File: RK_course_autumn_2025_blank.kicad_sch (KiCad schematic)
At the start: 13 parts, among them J1 JST-ZH 6pin, J2 JST-ZH 6pin, J3 Conn_01x02, J4 JST-ZH 6pin, J5 JST-ZH 6pin

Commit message: update
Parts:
- added R1: R, Resistor_SMD:R_0603_1608Metric_Pad0.98x0.95mm_HandSolder, symbol Device:R
- A2: footprint KURSUS:ESP32-S3-DevKitC-1 -> RK_COURSE:ESP32-S3-DevKitC-1
- U4, U6: footprint TANK:TB6612FNG_DUAL_MOTOR_DRIVER_RED -> KURSUS:TB6612FNG_DUAL_MOTOR_DRIVER_RED
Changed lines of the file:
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@@
 			)
 		)
-		(property "Footprint" "KURSUS:ESP32-S3-DevKitC-1"
+		(property "Footprint" "RK_COURSE:ESP32-S3-DevKitC-1"
 			(at 172.72 51.308 0)
 			(effects
@@
 				(path "/a85e8d7d-6e69-4ae0-af3b-65bd111e6aa4"
 					(reference "#PWR02")
-					(unit 1)
-				)
-			)
-		)
-	)
-	(symbol
-		(lib_id "Kursus:TB6612FNG_MOTOR_DRIVER_RED")
-		(at 152.4 78.74 0)
-		(unit 1)
-		(exclude_from_sim no)
-		(in_bom yes)
-		(on_board yes)
-		(dnp no)
-		(property "Reference" "U6"
-			(at 154.94 76.454 0)
-			(effects
-				(font
-					(size 1.27 1.27)
-				)
-			)
-		)
-		(property "Value" "~"
-			(at 152.4 76.2 0)
-			(effects
-				(font
-					(size 1.27 1.27)
-				)
-			)
-		)
-		(property "Footprint" "TANK:TB6612FNG_DUAL_MOTOR_DRIVER_RED"
-			(at 152.4 75.565 0)
-			(effects
-				(font
-					(size 1.27 1.27)
-				)
-				(hide yes)
-			)
-		)
-		(property "Datasheet" ""
-			(at 152.4 75.565 0)
-			(effects
-				(font
-					(size 1.27 1.27)
-				)
-				(hide yes)
-			)
-		)
-		(property "Description" ""
-			(at 152.4 75.565 0)
-			(effects
-				(font
-					(size 1.27 1.27)
-				)
-				(hide yes)
-			)
-		)
-		(pin "15"
-		)
-		(pin "14"
-		)
-		(pin "16"
-		)
-		(pin "1"
-		)
-		(pin "2"
-		)
-		(pin "10"
-		)
-		(pin "5"
-		)
-		(pin "6"
-		)
-		(pin "4"
-		)
-		(pin "9"
-		)
-		(pin "11"
-		)
-		(pin "8"
-		)
-		(pin "12"
-		)
-		(pin "7"
-		)
-		(pin "3"
-		)
-		(pin "13"
-		)
-		(instances
-			(project "RK_course_autumn_2025_blank"
-				(path "/a85e8d7d-6e69-4ae0-af3b-65bd111e6aa4"
-					(reference "U6")
 					(unit 1)
 				)
@@
 	)
 	(symbol
+		(lib_id "Device:R")
+		(at 71.12 27.94 0)
+		(unit 1)
+		(exclude_from_sim no)
+		(in_bom yes)
+		(on_board yes)
+		(dnp no)
+		(fields_autoplaced yes)
+		(property "Reference" "R1"
+			(at 73.66 26.6699 0)
+			(effects
+				(font
+					(size 1.27 1.27)
+				)
+				(justify left)
+			)
+		)
+		(property "Value" "R"
+			(at 73.66 29.2099 0)
+			(effects
+				(font
+					(size 1.27 1.27)
+				)
+				(justify left)
+			)
+		)
+		(property "Footprint" "Resistor_SMD:R_0603_1608Metric_Pad0.98x0.95mm_HandSolder"
+			(at 69.342 27.94 90)
+			(effects
+				(font
+					(size 1.27 1.27)
+				)
+				(hide yes)
+			)
+		)
+		(property "Datasheet" "~"
+			(at 71.12 27.94 0)
+			(effects
+				(font
+					(size 1.27 1.27)
+				)
+				(hide yes)
+			)
+		)
+		(property "Description" "Resistor"
+			(at 71.12 27.94 0)
+			(effects
+				(font
+					(size 1.27 1.27)
+				)
+				(hide yes)
+			)
+		)
+		(pin "1"
+		)
+		(pin "2"
+		)
+		(instances
+			(project ""
+				(path "/a85e8d7d-6e69-4ae0-af3b-65bd111e6aa4"
+					(reference "R1")
+					(unit 1)
+				)
+			)
+		)
+	)
+	(symbol
 		(lib_id "Kursus:PINGEREGU")
 		(at 43.18 26.67 0)
@@
 			)
 		)
-		(property "Footprint" "TANK:TB6612FNG_DUAL_MOTOR_DRIVER_RED"
+		(property "Footprint" "KURSUS:TB6612FNG_DUAL_MOTOR_DRIVER_RED"
 			(at 110.49 75.565 0)
 			(effects
@@
 					(unit 1)
 				)
+			)
+		)
+	)
+	(symbol
+		(lib_id "Kursus:TB6612FNG_MOTOR_DRIVER_RED")
+		(at 152.4 78.74 0)
+		(unit 1)
+		(exclude_from_sim no)
+		(in_bom yes)
+		(on_board yes)
+		(dnp no)
+		(property "Reference" "U6"
+			(at 154.94 76.454 0)
+			(effects
+				(font
+					(size 1.27 1.27)
+				)
+			)
+		)
+		(property "Value" "~"
+			(at 152.4 76.2 0)
+			(effects
+				(font
+					(size 1.27 1.27)
+				)
+			)
+		)
+		(property "Footprint" "KURSUS:TB6612FNG_DUAL_MOTOR_DRIVER_RED"
+			(at 152.4 75.565 0)
+			(effects
+				(font
+					(size 1.27 1.27)
+				)
+				(hide yes)
+			)
+		)
+		(property "Datasheet" ""
+			(at 152.4 75.565 0)
+			(effects
+				(font
+					(size 1.27 1.27)
+				)
+				(hide yes)
+			)
+		)
+		(property "Description" ""
+			(at 152.4 75.565 0)
+			(effects
+				(font
+					(size 1.27 1.27)
+				)
+				(hide yes)
+			)
+		)
+		(pin "15"
+		)
+		(pin "14"
+		)
+		(pin "16"
+		)
+		(pin "1"
+		)
+		(pin "2"
+		)
+		(pin "10"
+		)
+		(pin "5"
+		)
+		(pin "6"
+		)
+		(pin "4"
+		)
+		(pin "9"
+		)
+		(pin "11"
+		)
+		(pin "8"
+		)
+		(pin "12"
+		)
+		(pin "7"
+		)
+		(pin "3"
+		)
+		(pin "13"
+		)
+		(instances
+			(project "RK_course_autumn_2025_blank"
+				(path "/a85e8d7d-6e69-4ae0-af3b-65bd111e6aa4"
+					(reference "U6")
+					(unit 1)
+				)

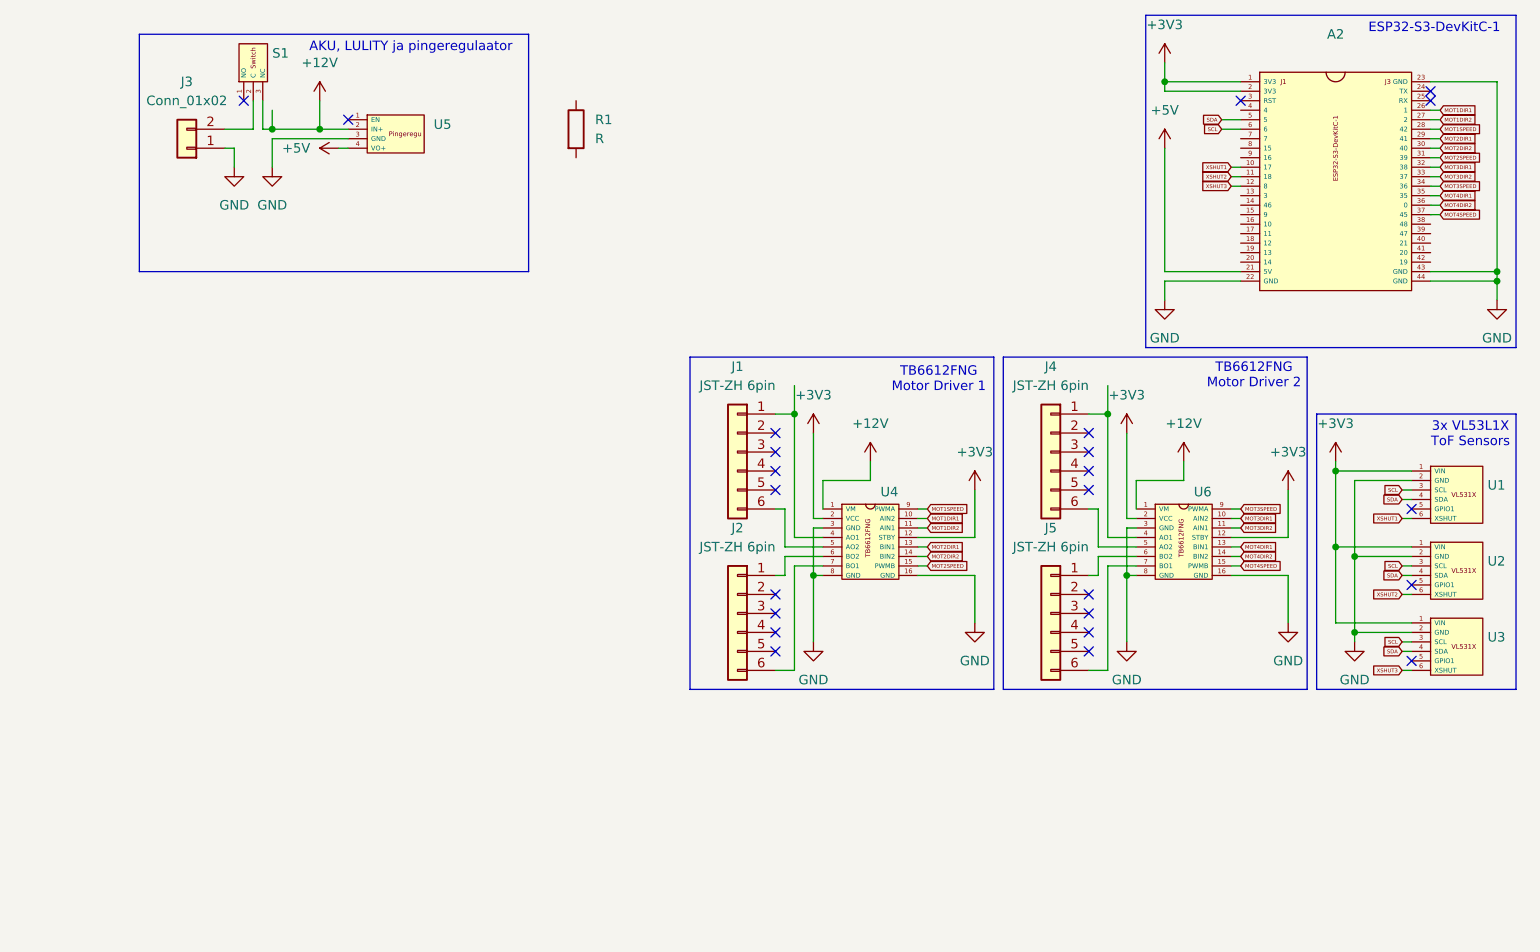
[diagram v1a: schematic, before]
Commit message: Added IMU footprint, model, schematic. Updated the schematic and PCB a bit
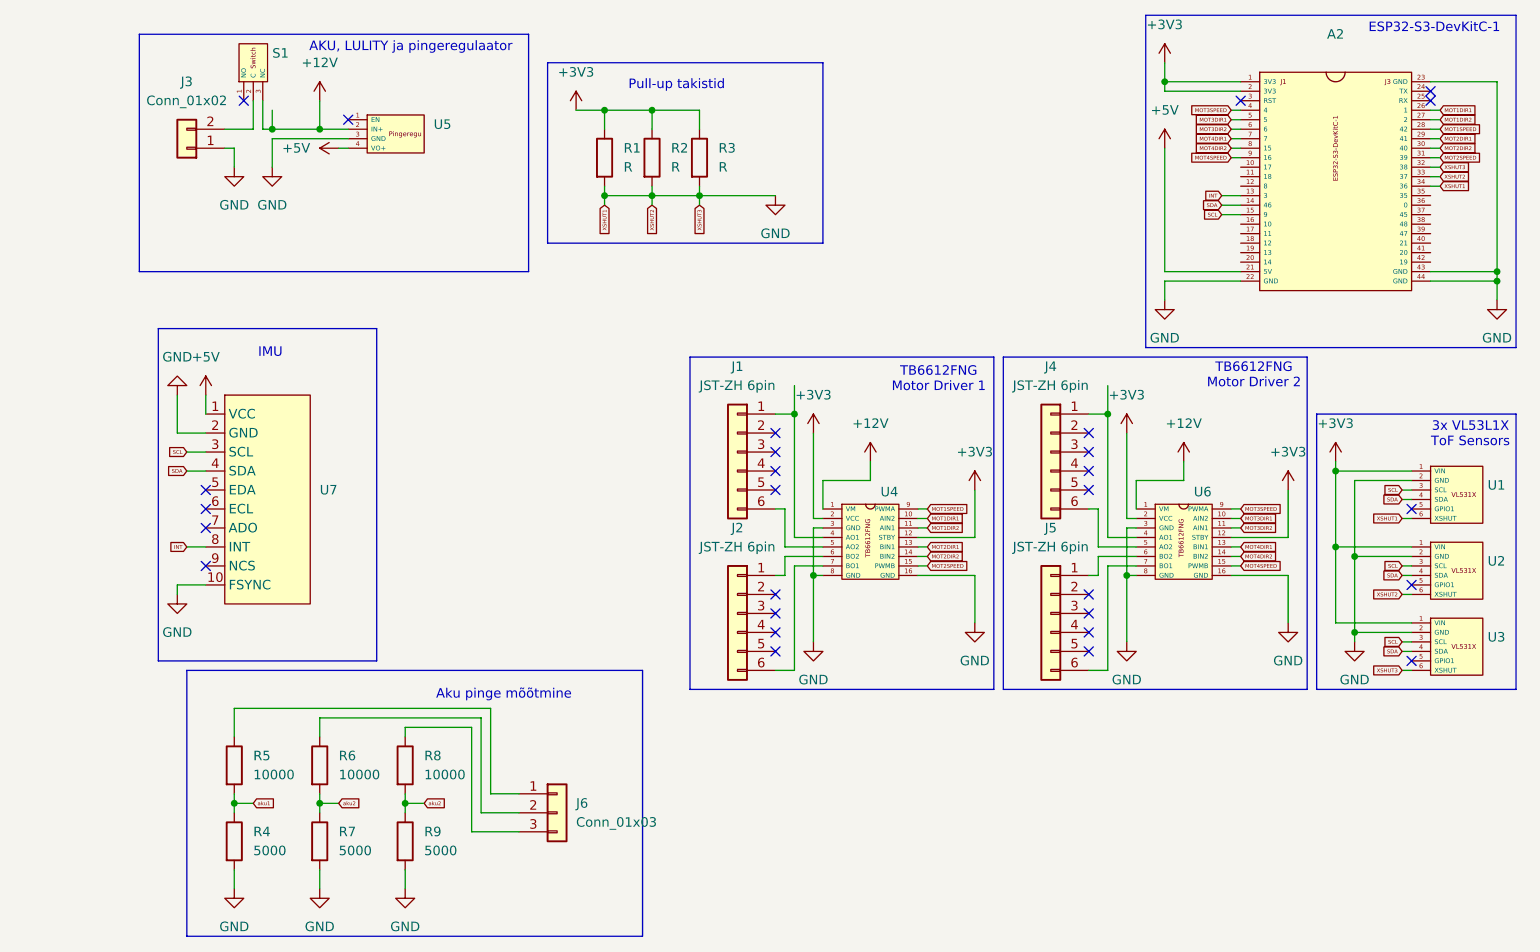
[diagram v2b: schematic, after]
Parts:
- added J6: Conn_01x03, symbol Connector_Generic:Conn_01x03
- added R2, R3: R, Resistor_SMD:R_0603_1608Metric_Pad0.98x0.95mm_HandSolder, symbol Device:R
- added R4, R7, R9: 5000, symbol Device:R
- added R5, R6, R8: 10000, symbol Device:R
- added U7: ~, KURSUS:IMU, symbol Kursus:IMU
- J1, J2, J4, J5: footprint Connector_JST:JST_ZH_B6B-ZR_1x06_P1.50mm_Vertical -> KURSUS:JST_ZH_B6B-ZR_1x06_P1.50mm_Vertical
- J3: footprint Connector_AMASS:AMASS_XT30PW-M_1x02_P2.50mm_Horizontal -> KURSUS:AMASS_XT30PW-M_1x02_P2.50mm_Horizontal
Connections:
- net +3V3: now also R1.1, R2.1, R3.1
- net +5V: now also U7.1 (VCC)
- net GND: now also A2.32 (38), A2.33 (37), A2.34 (36), R1.2, U1.6 (XSHUT), U2.6 (XSHUT), U3.6 (XSHUT), R2.2, R3.2, R4.2, R7.2, R9.2, U7.10 (FSYNC), U7.2 (GND)
- net MOT3DIR1: now also A2.5; no longer A2.32 (38)
- net MOT3DIR2: now also A2.6; no longer A2.33 (37)
- net MOT3SPEED: now also A2.4; no longer A2.34 (36)
- net MOT4DIR1: now also A2.7; no longer A2.35
- net MOT4DIR2: now also A2.8 (15); no longer A2.36 (0)
- net MOT4SPEED: now also A2.9 (16); no longer A2.37 (45)
- net SCL: now also A2.15 (9), U7.3 (SCL); no longer A2.6
- net SDA: now also A2.14 (46), U7.4 (SDA); no longer A2.5
- net INT: now reaches A2.13 (3)
- net INT: now also U7.8 (INT)
- net XSHUT1: no longer names the net of A2.10 (17)
- net XSHUT1: no longer U1.6 (XSHUT)
- net XSHUT2: no longer names the net of A2.11 (18)
- net XSHUT2: no longer U2.6 (XSHUT)
- net XSHUT3: no longer names the net of A2.12 (8)
- net XSHUT3: no longer U3.6 (XSHUT)
- new net: J6.1 (Pin_1), R5.1
- new net: J6.3 (Pin_3), R8.1
- new net: J6.2 (Pin_2), R6.1
- new net aku1: R4.1, R5.2
- new net aku2: R6.2, R7.1, R8.2, R9.1
- no-connect marks 24 -> 28
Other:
- note added: "Aku pinge mõõtmine"
- note added: "IMU"
- note added: "Pull-up takistid"
- moved on the sheet: R1

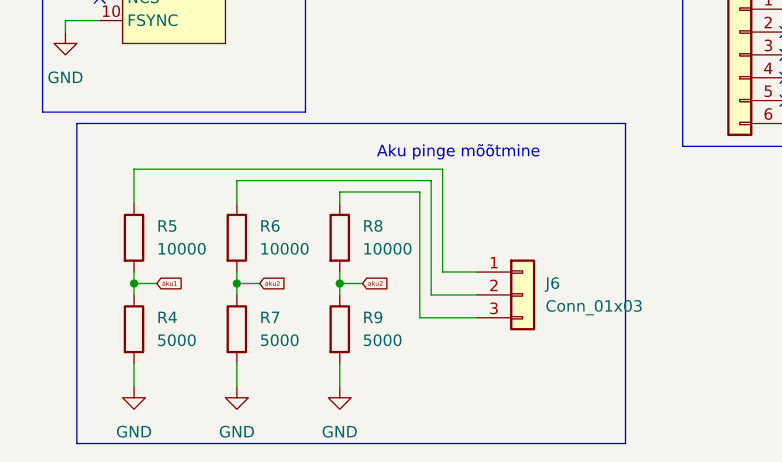
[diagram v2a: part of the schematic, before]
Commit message: Better placement for 12V
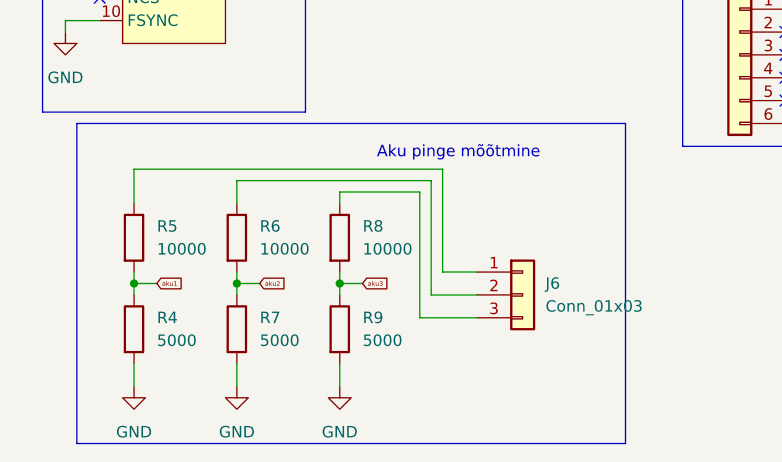
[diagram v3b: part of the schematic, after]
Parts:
- J6: footprint (none) -> Connector_PinHeader_2.54mm:PinHeader_1x03_P2.54mm_Vertical
- R4, R5, R6, R7, R8, R9: footprint (none) -> Resistor_SMD:R_0603_1608Metric_Pad0.98x0.95mm_HandSolder
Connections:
- net aku2: no longer R8.2, R9.1
- new net aku3: R8.2, R9.1
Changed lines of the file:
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@@
 	(wire
 		(pts
+			(xy 57.15 121.92) (xy 63.5 121.92)
+		)
+		(stroke
+			(width 0)
+			(type default)
+		)
+	)
+	(wire
+		(pts
 			(xy 181.61 97.79) (xy 182.88 97.79)
 		)
@@
 	(wire
 		(pts
-			(xy 57.15 121.92) (xy 63.5 121.92)
-		)
-		(stroke
-			(width 0)
-			(type default)
-		)
-	)
-	(wire
-		(pts
 			(xy 124.46 87.63) (xy 124.46 93.98)
 		)
@@
 		)
 	)
-	(global_label "aku2"
+	(global_label "aku3"
 		(shape input)
 		(at 50.8 118.11 0)
@@
 			)
 		)
-		(property "Footprint" ""
+		(property "Footprint" "Resistor_SMD:R_0603_1608Metric_Pad0.98x0.95mm_HandSolder"
 			(at 23.622 113.03 90)
 			(effects
@@
 			)
 		)
-		(property "Footprint" ""
+		(property "Footprint" "Resistor_SMD:R_0603_1608Metric_Pad0.98x0.95mm_HandSolder"
 			(at 46.482 123.19 90)
 			(effects
@@
 			)
 		)
-		(property "Footprint" ""
+		(property "Footprint" "Resistor_SMD:R_0603_1608Metric_Pad0.98x0.95mm_HandSolder"
 			(at 46.482 113.03 90)
 			(effects
@@
 	)
 	(symbol
-		(lib_id "power:+3V3")
-		(at 71.12 25.4 0)
-		(unit 1)
-		(exclude_from_sim no)
-		(in_bom yes)
-		(on_board yes)
-		(dnp no)
-		(fields_autoplaced yes)
-		(property "Reference" "#PWR028"
-			(at 71.12 29.21 0)
-			(effects
-				(font
-					(size 1.27 1.27)
-				)
-				(hide yes)
-			)
-		)
-		(property "Value" "+3V3"
-			(at 71.12 20.32 0)
-			(effects
-				(font
-					(size 1.27 1.27)
-				)
-			)
-		)
-		(property "Footprint" ""
-			(at 71.12 25.4 0)
-			(effects
-				(font
-					(size 1.27 1.27)
-				)
-				(hide yes)
-			)
-		)
-		(property "Datasheet" ""
-			(at 71.12 25.4 0)
-			(effects
-				(font
-					(size 1.27 1.27)
-				)
-				(hide yes)
-			)
-		)
-		(property "Description" "Power symbol creates a global label with name \"+3V3\""
-			(at 71.12 25.4 0)
-			(effects
-				(font
-					(size 1.27 1.27)
-				)
-				(hide yes)
-			)
-		)
-		(pin "1"
-		)
-		(instances
-			(project ""
-				(path "/a85e8d7d-6e69-4ae0-af3b-65bd111e6aa4"
-					(reference "#PWR028")
-					(unit 1)
-				)
-			)
-		)
-	)
-	(symbol
 		(lib_id "Device:R")
 		(at 36.83 123.19 0)
@@
 			)
 		)
-		(property "Footprint" ""
+		(property "Footprint" "Resistor_SMD:R_0603_1608Metric_Pad0.98x0.95mm_HandSolder"
 			(at 35.052 123.19 90)
 			(effects
@@
 			)
 		)
-		(property "Footprint" ""
+		(property "Footprint" "Resistor_SMD:R_0603_1608Metric_Pad0.98x0.95mm_HandSolder"
 			(at 35.052 113.03 90)
 			(effects
@@
 			)
 		)
-		(property "Footprint" ""
+		(property "Footprint" "Connector_PinHeader_2.54mm:PinHeader_1x03_P2.54mm_Vertical"
 			(at 68.58 119.38 0)
 			(effects
@@
 	)
 	(symbol
+		(lib_id "power:+3V3")
+		(at 71.12 25.4 0)
+		(unit 1)
+		(exclude_from_sim no)
+		(in_bom yes)
+		(on_board yes)
+		(dnp no)
+		(fields_autoplaced yes)
+		(property "Reference" "#PWR028"
+			(at 71.12 29.21 0)
+			(effects
+				(font
+					(size 1.27 1.27)
+				)
+				(hide yes)
+			)
+		)
+		(property "Value" "+3V3"
+			(at 71.12 20.32 0)
+			(effects
+				(font
+					(size 1.27 1.27)
+				)
+			)
+		)
+		(property "Footprint" ""
+			(at 71.12 25.4 0)
+			(effects
+				(font
+					(size 1.27 1.27)
+				)
+				(hide yes)
+			)
+		)
+		(property "Datasheet" ""
+			(at 71.12 25.4 0)
+			(effects
+				(font
+					(size 1.27 1.27)
+				)
+				(hide yes)
+			)
+		)
+		(property "Description" "Power symbol creates a global label with name \"+3V3\""
+			(at 71.12 25.4 0)
+			(effects
+				(font
+					(size 1.27 1.27)
+				)
+				(hide yes)
+			)
+		)
+		(pin "1"
+		)
+		(instances
+			(project ""
+				(path "/a85e8d7d-6e69-4ae0-af3b-65bd111e6aa4"
+					(reference "#PWR028")
+					(unit 1)
+				)
+			)
+		)
+	)
+	(symbol
 		(lib_id "Device:R")
 		(at 25.4 123.19 0)
@@
 			)
 		)
-		(property "Footprint" ""
+		(property "Footprint" "Resistor_SMD:R_0603_1608Metric_Pad0.98x0.95mm_HandSolder"
 			(at 23.622 123.19 90)
 			(effects
